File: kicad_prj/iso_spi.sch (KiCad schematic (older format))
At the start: 21 parts

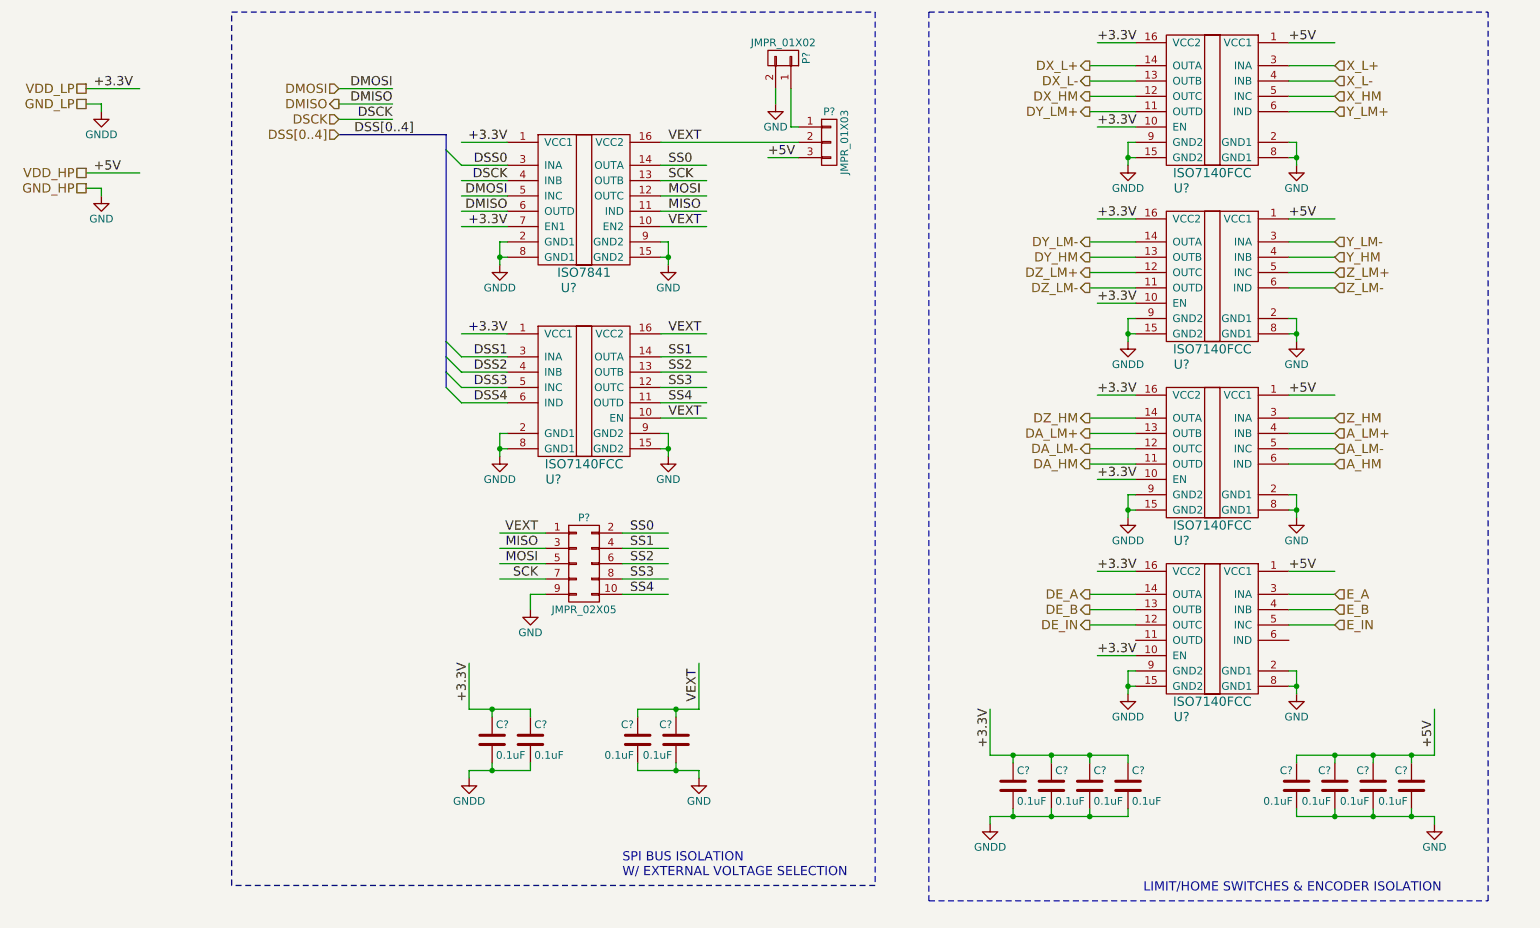
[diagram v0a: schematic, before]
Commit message: Schematics 7
Started power schematics.
Need to:
- correct symbol for sw vreg
- add regulator for 3.3V digital side
- indicate which voltages go to which circuit
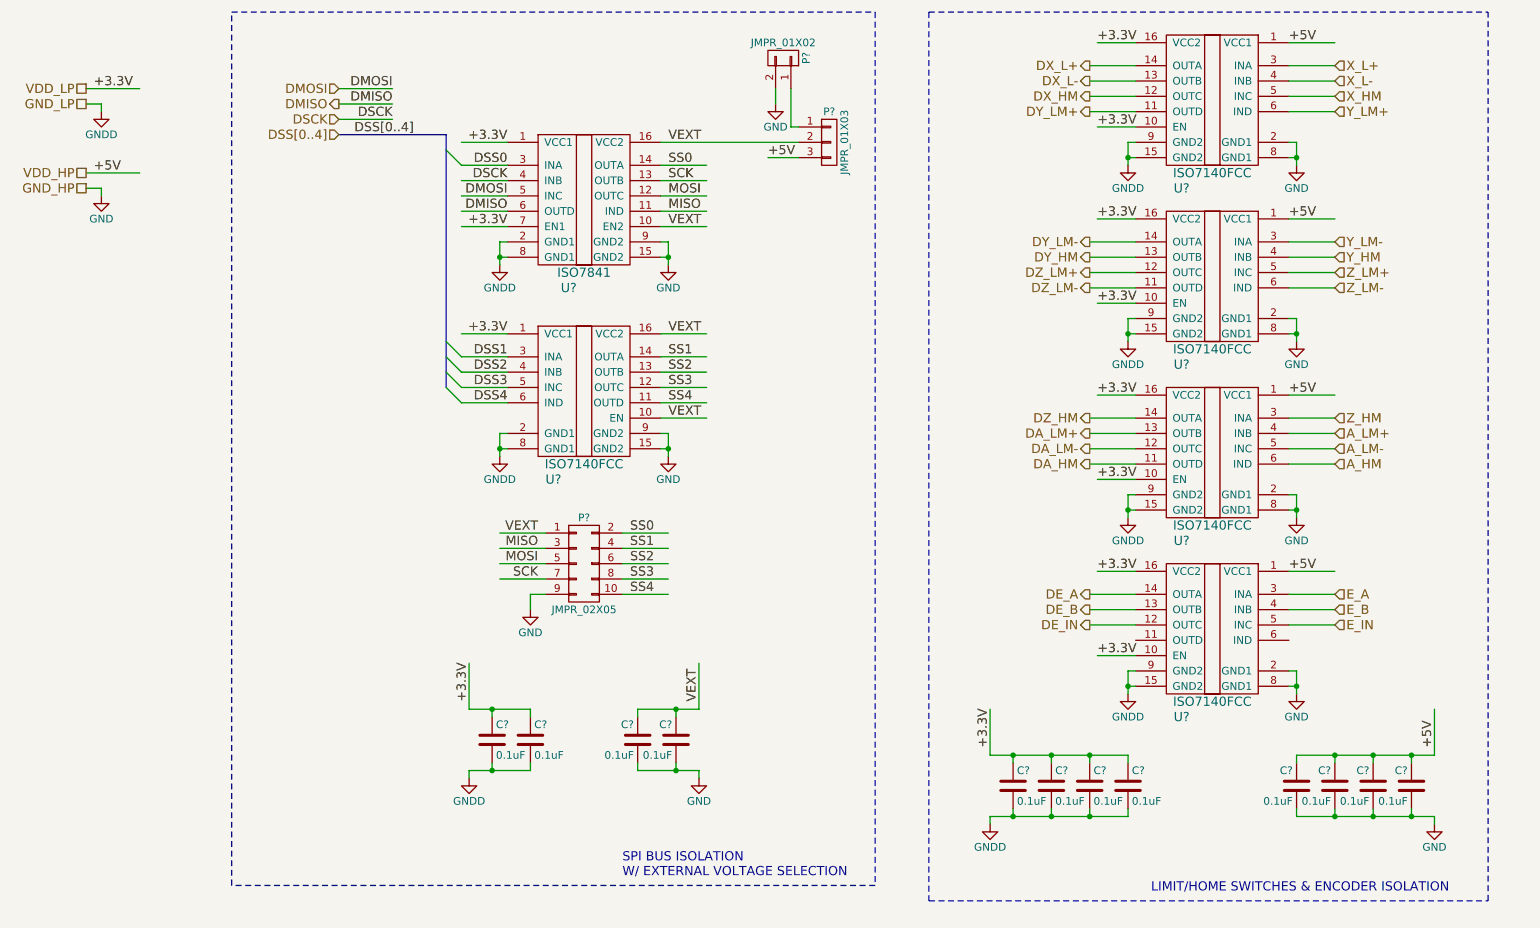
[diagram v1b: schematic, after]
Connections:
- wire segments 193 -> 165
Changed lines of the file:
@@
 $Descr A4 11693 8268
 encoding utf-8
-Sheet 10 10
+Sheet 10 11
 Title ""
 Date ""
@@
 $EndComp
 Wire Wire Line
-	3950 5150 4100 5150
-Wire Wire Line
-	4100 5150 4350 5150
+	3950 5150 4350 5150
 Wire Wire Line
 	3950 5150 3950 4850
 Wire Wire Line
-	3950 5550 4100 5550
-Wire Wire Line
-	4100 5550 4350 5550
+	3950 5550 4350 5550
 Wire Wire Line
 	3950 5550 3950 5600
@@
 VEXT
 Wire Wire Line
-	5050 5150 5300 5150
-Wire Wire Line
-	5300 5150 5450 5150
+	5050 5150 5450 5150
 Wire Wire Line
 	5450 5150 5450 4850
 Wire Wire Line
-	5050 5550 5300 5550
-Wire Wire Line
-	5300 5550 5450 5550
+	5050 5550 5450 5550
 Wire Wire Line
 	5450 5550 5450 5600
@@
 	4200 3150 3900 3150
 Wire Bus Line
-	3800 1400 3800 1500
-Wire Bus Line
-	3800 1500 3800 2750
-Wire Bus Line
-	3800 2750 3800 2850
-Wire Bus Line
-	3800 2850 3800 2950
-Wire Bus Line
-	3800 2950 3800 3050
+	3800 1400 3800 3050
 Wire Wire Line
 	5200 3250 5500 3250
@@
 	5200 3350 5250 3350
 Wire Wire Line
-	5250 3350 5250 3450
-Wire Wire Line
-	5250 3450 5250 3500
+	5250 3350 5250 3500
 Wire Wire Line
 	5200 3450 5250 3450
@@
 	4200 3350 4150 3350
 Wire Wire Line
-	4150 3350 4150 3450
-Wire Wire Line
-	4150 3450 4150 3500
+	4150 3350 4150 3500
 Wire Wire Line
 	4200 3450 4150 3450
@@
 	4200 2100 4150 2100
 Wire Wire Line
-	4150 2100 4150 2200
-Wire Wire Line
-	4150 2200 4150 2250
+	4150 2100 4150 2250
 Wire Wire Line
 	4200 2200 4150 2200
@@
 	5200 2100 5250 2100
 Wire Wire Line
-	5250 2100 5250 2200
-Wire Wire Line
-	5250 2200 5250 2250
+	5250 2100 5250 2250
 Wire Wire Line
 	5200 2200 5250 2200
@@
 	9300 1450 9350 1450
 Wire Wire Line
-	9350 1450 9350 1550
-Wire Wire Line
-	9350 1550 9350 1600
+	9350 1450 9350 1600
 Wire Wire Line
 	9300 1550 9350 1550
@@
 	8300 1450 8250 1450
 Wire Wire Line
-	8250 1450 8250 1550
-Wire Wire Line
-	8250 1550 8250 1600
+	8250 1450 8250 1600
 Wire Wire Line
 	8300 1550 8250 1550
@@
 	9300 2600 9350 2600
 Wire Wire Line
-	9350 2600 9350 2700
-Wire Wire Line
-	9350 2700 9350 2750
+	9350 2600 9350 2750
 Wire Wire Line
 	9300 2700 9350 2700
@@
 	8300 2600 8250 2600
 Wire Wire Line
-	8250 2600 8250 2700
-Wire Wire Line
-	8250 2700 8250 2750
+	8250 2600 8250 2750
 Wire Wire Line
 	8300 2700 8250 2700
@@
 	9300 3750 9350 3750
 Wire Wire Line
-	9350 3750 9350 3850
-Wire Wire Line
-	9350 3850 9350 3900
+	9350 3750 9350 3900
 Wire Wire Line
 	9300 3850 9350 3850
@@
 	8300 3750 8250 3750
 Wire Wire Line
-	8250 3750 8250 3850
-Wire Wire Line
-	8250 3850 8250 3900
+	8250 3750 8250 3900
 Wire Wire Line
 	8300 3850 8250 3850
@@
 	9300 4900 9350 4900
 Wire Wire Line
-	9350 4900 9350 5000
-Wire Wire Line
-	9350 5000 9350 5050
+	9350 4900 9350 5050
 Wire Wire Line
 	9300 5000 9350 5000
@@
 	8300 4900 8250 4900
 Wire Wire Line
-	8250 4900 8250 5000
-Wire Wire Line
-	8250 5000 8250 5050
+	8250 4900 8250 5050
 Wire Wire Line
 	8300 5000 8250 5000
@@
 Connection ~ 8000 5850
 Wire Wire Line
-	8250 5800 8250 5850
-Wire Wire Line
-	8250 5500 8250 5450
+	8250 5850 8250 5800
+Wire Wire Line
+	8250 5450 8250 5500
 Wire Wire Line
 	8000 5500 8000 5450
@@
 	10250 5850 10250 5900
 Wire Wire Line
-	10100 5500 10100 5450
+	10100 5450 10100 5500
 Connection ~ 10100 5450
 Wire Wire Line
-	10100 5800 10100 5850
+	10100 5850 10100 5800
 Connection ~ 10100 5850
 Wire Wire Line
-	9850 5800 9850 5850
+	9850 5850 9850 5800
 Connection ~ 9850 5850
 Wire Wire Line
@@
 Connection ~ 9600 5450
 Wire Wire Line
-	9850 5500 9850 5450
+	9850 5450 9850 5500
 Connection ~ 9850 5450
 $Comp
@@
 $EndComp
 Wire Wire Line
-	8250 5450 8000 5450
-Wire Wire Line
-	8000 5450 7750 5450
-Wire Wire Line
-	7750 5450 7500 5450
-Wire Wire Line
-	7500 5450 7350 5450
-Wire Wire Line
-	8250 5850 8000 5850
-Wire Wire Line
-	8000 5850 7750 5850
-Wire Wire Line
-	7750 5850 7500 5850
-Wire Wire Line
-	7500 5850 7350 5850
-Wire Wire Line
-	9350 5450 9600 5450
-Wire Wire Line
-	9600 5450 9850 5450
-Wire Wire Line
-	9850 5450 10100 5450
-Wire Wire Line
-	10100 5450 10250 5450
-Wire Wire Line
-	9350 5850 9600 5850
-Wire Wire Line
-	9600 5850 9850 5850
-Wire Wire Line
-	9850 5850 10100 5850
-Wire Wire Line
-	10100 5850 10250 5850
+	7350 5450 8250 5450
+Wire Wire Line
+	7350 5850 8250 5850
+Wire Wire Line
+	9350 5450 10250 5450
+Wire Wire Line
+	9350 5850 10250 5850
 Text HLabel 8000 950  0    60   Output ~ 0
 DX_L+
@@
 Wire Notes Line
 	10600 6400 10600 600
-Text Notes 8350 6350 0    60   ~ 0
+Text Notes 8400 6350 0    60   ~ 0
 LIMIT/HOME SWITCHES & ENCODER ISOLATION
 $EndSCHEMATC

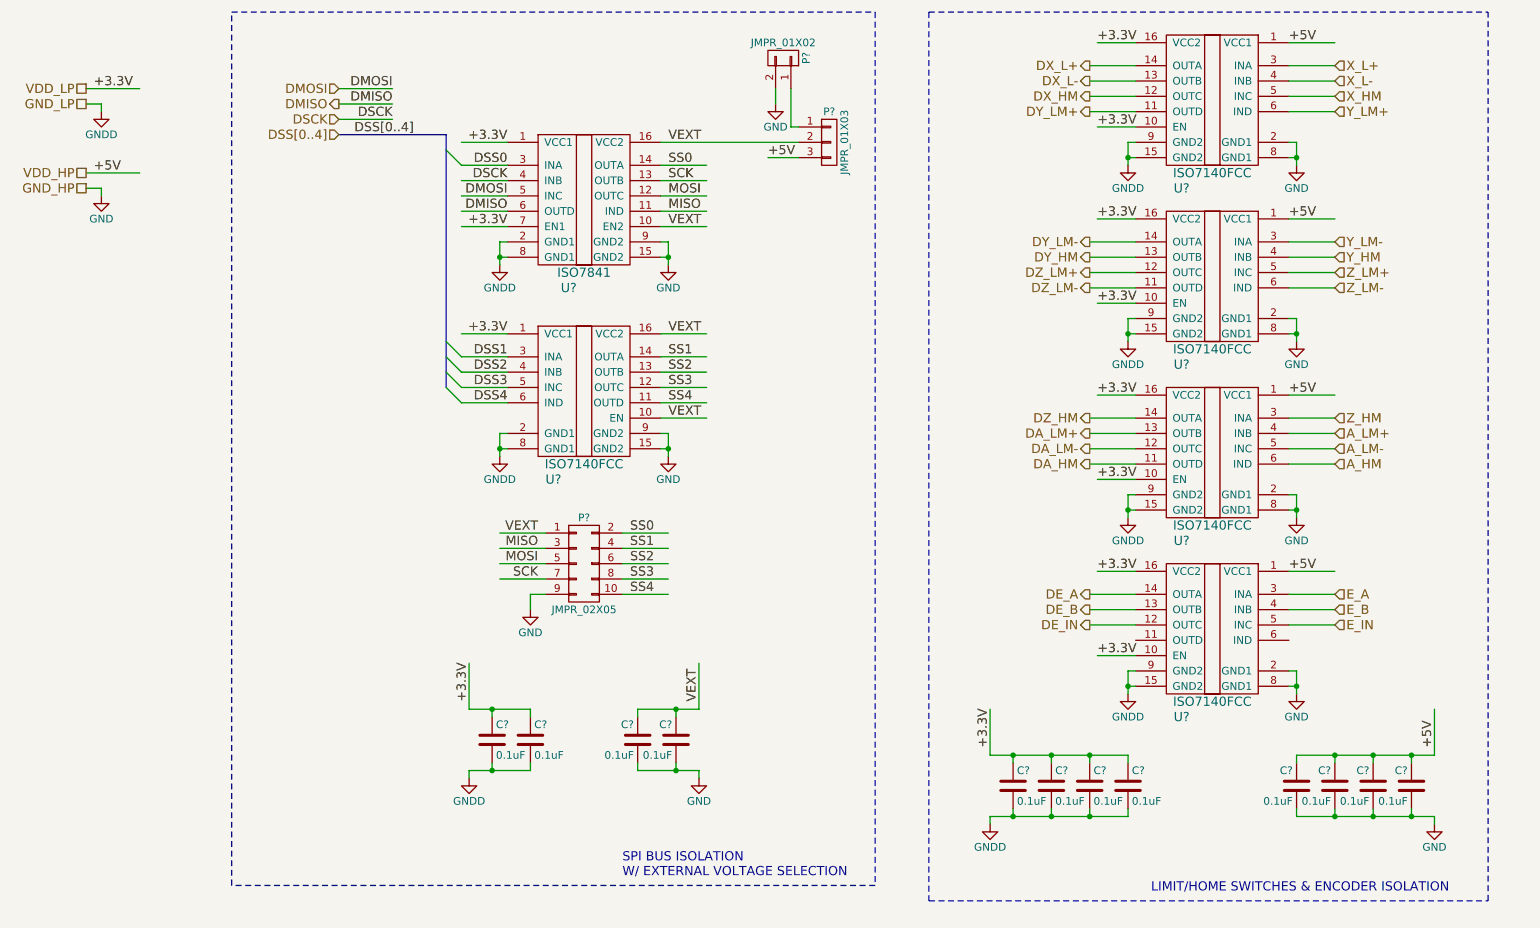
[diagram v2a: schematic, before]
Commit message: Corrected sheet sizes
A4 to A size on all sheets
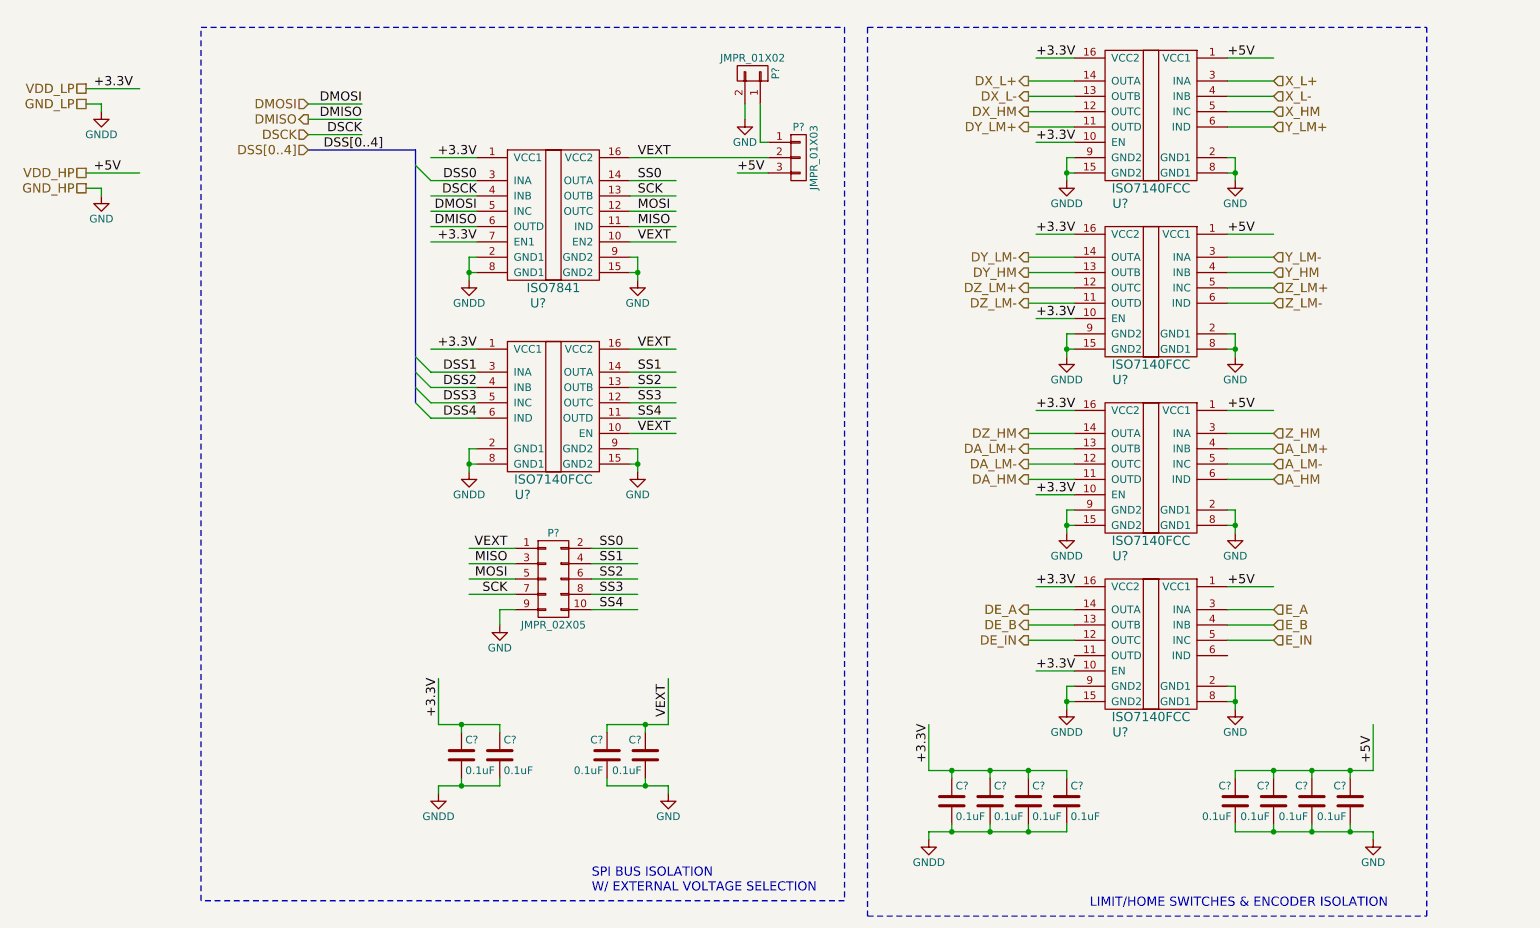
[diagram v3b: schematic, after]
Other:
- moved on the sheet: C?, P?, U?
